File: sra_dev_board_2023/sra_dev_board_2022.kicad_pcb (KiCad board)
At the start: 2 copper layers, 81.2 x 92.7 mm, 181 parts, among them J1 Conn_01x19_Male, J10 Conn_01x03_Male, J11 Conn_01x05_Male, J12 Conn_01x05_Male, J13 Conn_01x05_Male, J14 Conn_01x03_Male, J15 Conn_01x03_Male, J16 Screw_Terminal_01x05, J2 Conn_01x03_Male, J3 Conn_01x03_Male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

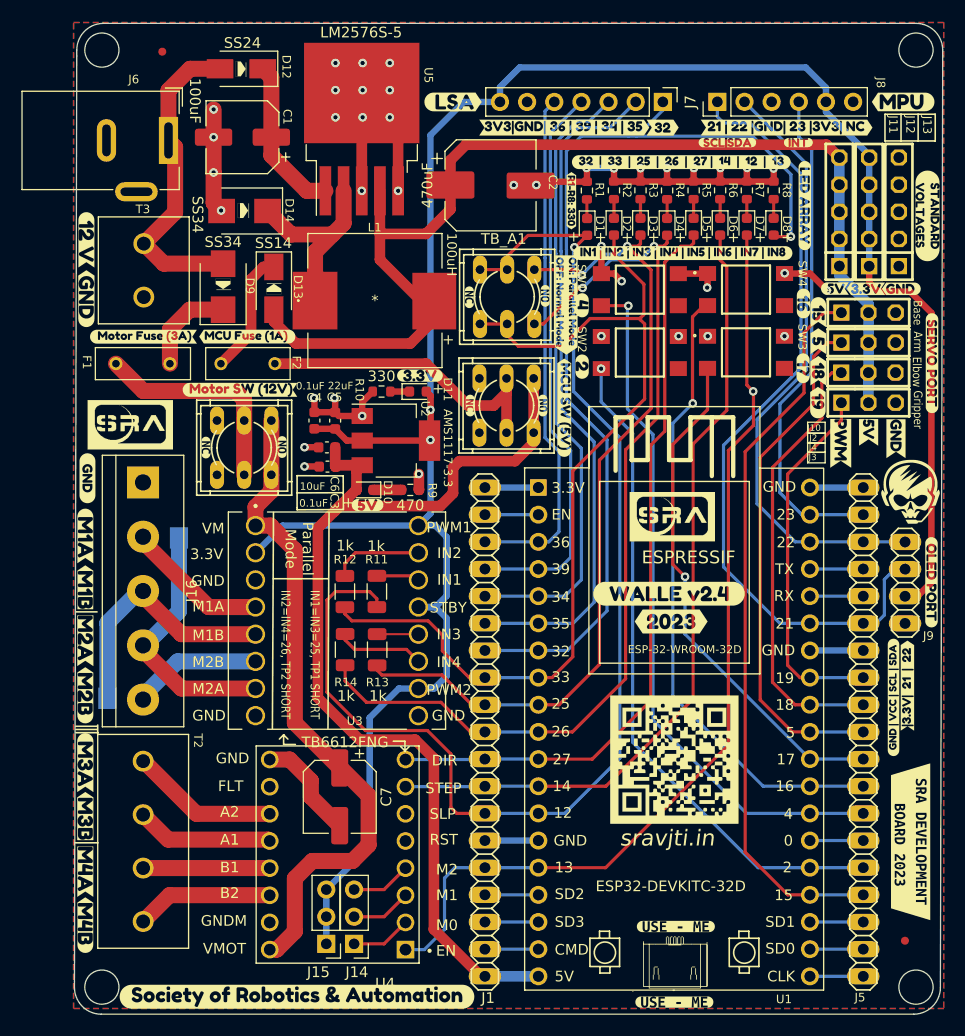
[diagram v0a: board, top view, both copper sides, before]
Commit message: Updated gerbers for LSA and SRA-Board
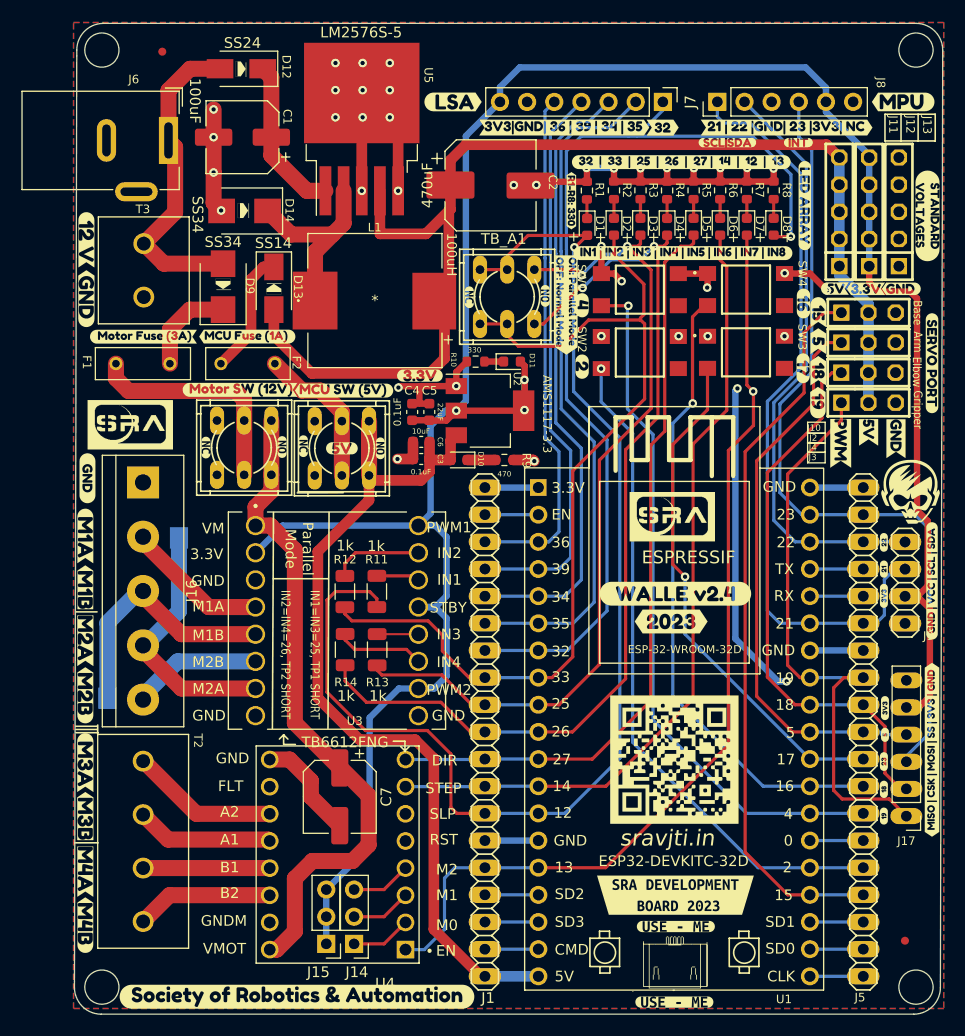
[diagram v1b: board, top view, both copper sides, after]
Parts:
- removed the kibuzzard-61F6A786 at (149.9, 81.7)
- removed the kibuzzard-61F792D2 at (146.8, 92.8)
- removed kibuzzard-61F79319 (x2): G***, kibuzzard-61F79319
- added J17: Conn_01x06_Male, Connector_PinHeader_2.54mm:PinHeader_1x06_P2.54mm_Vertical, F.Cu at (147.6, 103.6)
- added kibuzzard-63775DBB: G***, kibuzzard-63775DBB, F.Cu at (150.0, 97.4)
- added kibuzzard-63777F1B: G***, kibuzzard-63777F1B, B.Cu at (150.0, 97.4)
- added kibuzzard-6379FAF8: G***, kibuzzard-6379FAF8, F.Cu at (145.5, 78.0)
- added kibuzzard-6379FAF8: G***, kibuzzard-6379FAF8, B.Cu at (145.5, 78.0)
- added kibuzzard-6379FB2C: G***, kibuzzard-6379FB2C, F.Cu at (145.5, 80.5)
- added kibuzzard-6379FB2C: G***, kibuzzard-6379FB2C, B.Cu at (145.5, 80.5)
- added kibuzzard-6379FB66: G***, kibuzzard-6379FB66, F.Cu at (145.6, 93.5)
- added kibuzzard-6379FB66: G***, kibuzzard-6379FB66, F.Cu at (145.5, 83.0)
- added kibuzzard-6379FB66: G***, kibuzzard-6379FB66, B.Cu at (145.5, 83.0)
- added kibuzzard-6379FB66: G***, kibuzzard-6379FB66, B.Cu at (145.6, 93.5)
- added kibuzzard-6379FB9D: G***, kibuzzard-6379FB9D, F.Cu at (145.6, 96.0)
- added kibuzzard-6379FB9D: G***, kibuzzard-6379FB9D, B.Cu at (145.6, 96.0)
- added kibuzzard-6379FBC7: G***, kibuzzard-6379FBC7, F.Cu at (145.5, 98.5)
- added kibuzzard-6379FBC7: G***, kibuzzard-6379FBC7, B.Cu at (145.5, 98.5)
- added kibuzzard-6379FBDB: G***, kibuzzard-6379FBDB, F.Cu at (145.5, 101.1)
- added kibuzzard-6379FBDB: G***, kibuzzard-6379FBDB, B.Cu at (145.5, 101.1)
- added kibuzzard-6379FC14: G***, kibuzzard-6379FC14, F.Cu at (145.5, 103.6)
- added kibuzzard-6379FC14: G***, kibuzzard-6379FC14, B.Cu at (145.5, 103.6)
- added kibuzzard-6379FDB8: G***, kibuzzard-6379FDB8, B.Cu at (145.5, 85.6)
- added kibuzzard-6379FDB8: G***, kibuzzard-6379FDB8, B.Cu at (145.6, 90.9)
- moved kibuzzard-63707CFB 71.5 mm to (107.8, 48.0), turned to 180 degrees
- moved kibuzzard-63707B42 22.6 mm to (126.0, 111.0), turned to 0 degrees
- moved kibuzzard-61F7105E 20.7 mm to (95.0, 63.8), turned to 0 degrees
- moved REF** 19.4 mm to (76.6, 66.2)
- moved kibuzzard-61F6B86D 16.1 mm to (91.2, 69.0)
- moved 5V_SW1 15.9 mm to (94.8, 69.2)
- moved kibuzzard-61F6B878 15.7 mm to (98.4, 69.2)
- moved kibuzzard-61F792D2 11.5 mm to (150.0, 81.6)
- moved D11 9.23 mm to (110.7, 61.1)
- moved U2 9.23 mm to (108.7, 65.7)
- moved D10 9.23 mm to (105.8, 70.3)
- moved R10 9.23 mm to (107.3, 61.1)
- moved R9 9.23 mm to (110.0, 70.3)
- moved C4 9.18 mm to (101.4, 65.8)
- moved C5 8.84 mm to (103.0, 65.8)
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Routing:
- net GND: track 115.9 -> 148.1 mm
- net /23: track 46.9 -> 76.4 mm
- net /19: track 34.2 -> 54.8 mm
- net Net-(5V_SW1-Pad2): track 30.2 -> 14.1 mm
- net /5V_P: track 96.4 -> 82.2 mm
- net /3V3: track 217.4 -> 230.6 mm, vias 2 -> 3
- net /18: track 41.5 -> 51.7 mm
- net /5V: track 106.3 -> 113.4 mm
- net /5: track 48.2 -> 52.6 mm
- net /21: track 74.4 -> 71.0 mm
- net /22: track 57.2 -> 55.9 mm
- net Net-(12V_SW1-Pad2): track 20.4 -> 21.2 mm
